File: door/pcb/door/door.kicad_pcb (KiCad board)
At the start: 2 copper layers, 73.2 x 35.1 mm, 43 parts, among them J1 USB_B_Micro, J2 Conn_01x06_Male, J3 DB9_Female_MountingHoles, J4 Conn_01x03_Male, J5 Screw_Terminal_01x02, J6 Screw_Terminal_01x02, U1 10uF, U2 STM32F303CBTx, U3 SN65HVD230, Y1 8 Mhz

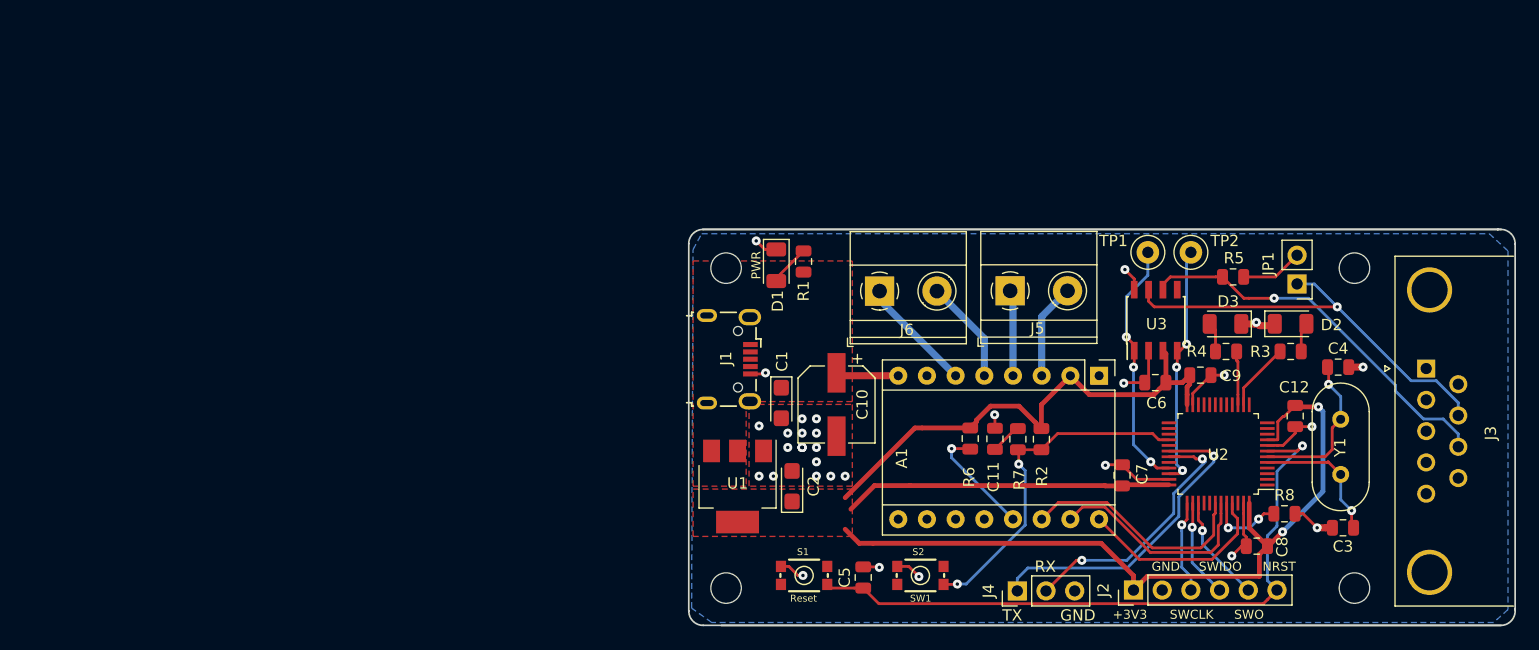
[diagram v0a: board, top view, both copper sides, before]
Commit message: recplaced usb micro jack with barrel-jack, reworked pcb layout
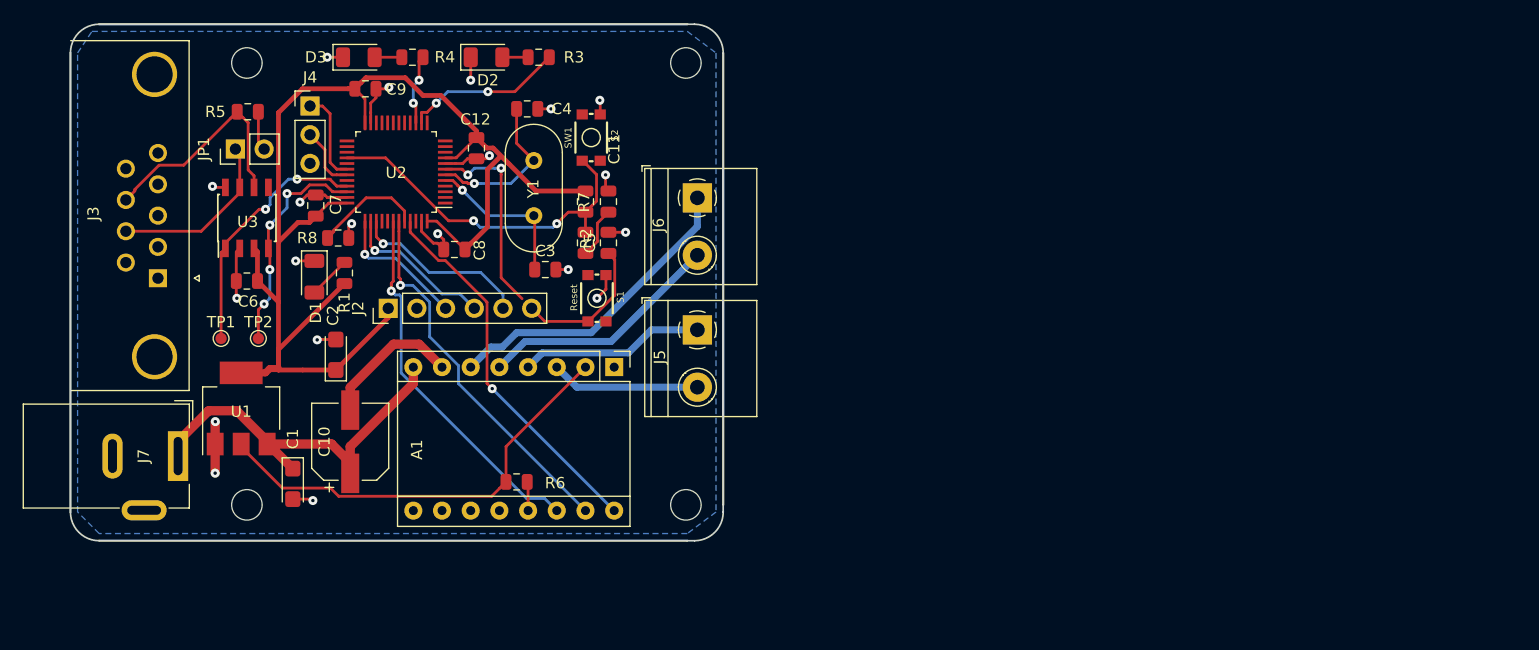
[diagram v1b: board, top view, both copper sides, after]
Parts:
- removed J1: USB_B_Micro, Connector_USB:USB_Micro-B_Wuerth_629105150521
- removed the REF** at (208.3, 121.7)
- removed the REF** at (208.3, 93.3)
- added J7: Power_in, Connector_BarrelJack:BarrelJack_Wuerth_6941xx301002, F.Cu at (104.1, 110.0)
- added REF**: MountingHole_2.7mm_M2.5, MountingHole:MountingHole_2.7mm_M2.5, F.Cu at (149.1, 114.3)
- added REF**: MountingHole_2.7mm_M2.5, MountingHole:MountingHole_2.7mm_M2.5, F.Cu at (149.1, 75.2)
- TP1, TP2: footprint TestPoint:TestPoint_Loop_D1.80mm_Drill1.0mm_Beaded -> TestPoint:TestPoint_Pad_D1.0mm
- moved J3 112.6 mm to (102.4, 94.2), turned to 270 degrees
- moved JP1 94.7 mm to (109.2, 82.8), turned to 90 degrees
- moved R5 88.4 mm to (110.3, 79.5)
- moved R8 87.3 mm to (118.3, 90.7)
- moved TP2 82.9 mm to (111.3, 99.6)
- moved TP1 82.4 mm to (108.0, 99.6)
- moved U3 81.0 mm to (110.2, 88.9)
- moved C6 80.9 mm to (110.2, 94.5)
- moved D3 80.3 mm to (120.1, 74.7), turned to 0 degrees
- moved C9 78.1 mm to (120.7, 77.5)
- moved U2 76.9 mm to (123.4, 84.8)
- moved R4 76.6 mm to (124.9, 74.7)
- moved C12 76.3 mm to (130.6, 82.7)
- moved J4 75.9 mm to (115.8, 79.0), turned to 0 degrees
- moved C8 75.7 mm to (128.6, 91.7)
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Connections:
- A1 pad 8: +5V -> +9V
- C1 pad 1: +5V -> +9V
- C10 pad 1: +5V -> +9V
- R1 pad 1: +5V -> +3V3
- U1 pad 3: +5V -> +9V
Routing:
- net +9V: track 0.00 -> 35.6 mm
- net NRST: track 58.8 -> 30.4 mm, vias 1 -> 2
- net /mcu/CANH: track 37.7 -> 15.5 mm, vias 1 -> 0
- net USART1_TX: track 28.4 -> 8.12 mm, vias 1 -> 0
- net USART1_RX: track 23.3 -> 5.67 mm, vias 2 -> 0
- net /motor/2B: track 10.3 -> 27.8 mm
- net DIR: track 17.6 -> 33.4 mm, vias 0 -> 1
- net STEP: track 19.3 -> 33.1 mm, vias 0 -> 1
- net /mcu/CANL: track 34.1 -> 20.5 mm, vias 1 -> 0
- net GND: track 47.1 -> 60.3 mm, vias 32 -> 20
- net /motor/2A: track 9.23 -> 21.6 mm
- net SLEEP: track 20.9 -> 32.9 mm, vias 0 -> 1
- net +3V3: track 143.1 -> 155.1 mm, vias 2 -> 0
- net /motor/1A: track 7.62 -> 16.4 mm
- net LED1: track 6.06 -> 14.2 mm, vias 0 -> 2
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- removed copper zone on F.Cu, net +3V3
- removed copper zone on F.Cu, net +5V
- removed copper zone on F.Cu, net GND
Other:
- board size 73.2 x 35.1 mm -> 57.8 x 45.7 mm
- net class +9V added: clearance 0.1524, trace_width 0.625, via_dia 0.8, via_drill 0.3
- board text removed: "+3V3"
- board text removed: "1A"
- board text removed: "1B"
- board text removed: "2A"
- board text removed: "2B"
- board text removed: "GND"
- board text removed: "NRST"
- board text removed: "PWR"
- board text removed: "RX"
- board text removed: "SWCLK"
- board text removed: "SWIDO"
- board text removed: "SWO"
- board text removed: "TX"
- board text removed: "Türsteuerung V0.1"

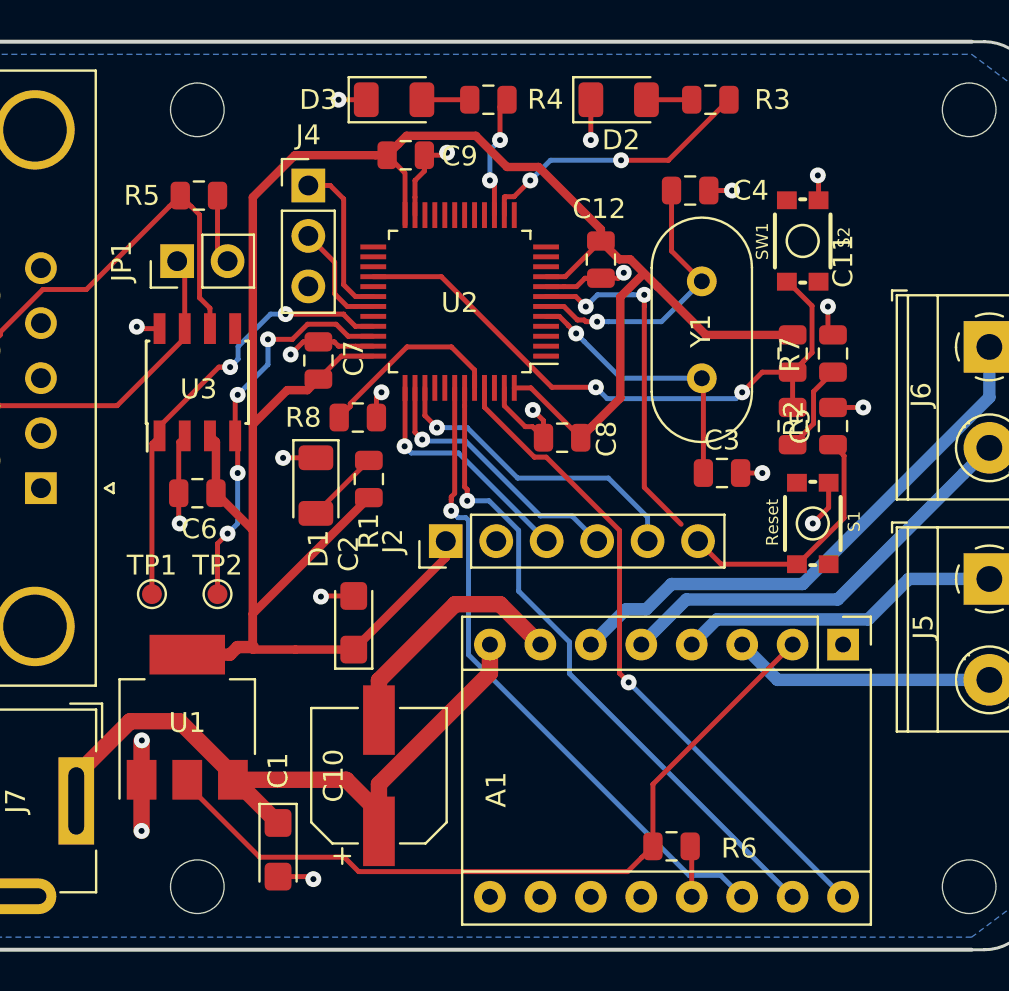
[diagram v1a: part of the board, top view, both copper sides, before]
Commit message: labeling and trackwidth
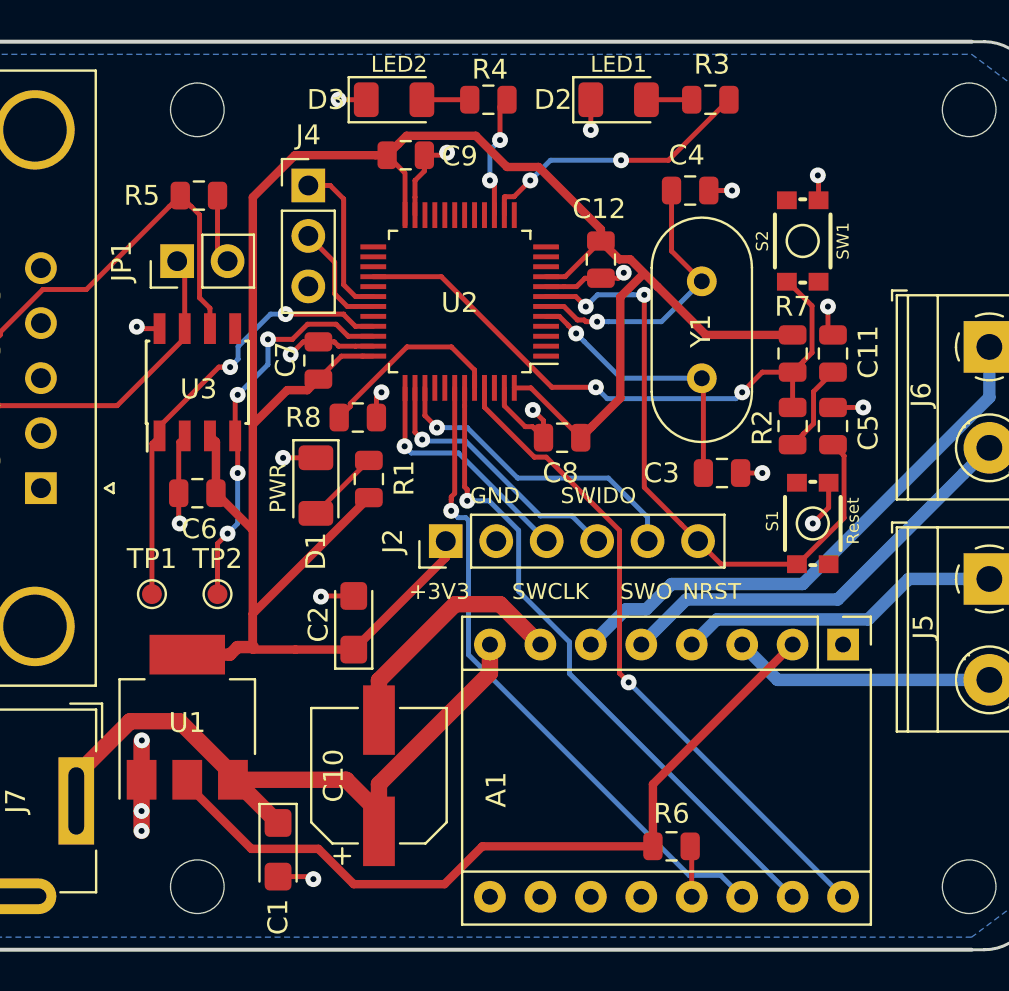
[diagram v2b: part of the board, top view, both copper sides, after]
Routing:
- net NRST: track 30.4 -> 31.6 mm
- net +3V3: track 155.1 -> 155.7 mm
- net GND: track 60.3 -> 59.8 mm, vias 20 -> 21
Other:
- board text added: "+3V3"
- board text added: "1A"
- board text added: "1B"
- board text added: "2A"
- board text added: "2B"
- board text added: "GND"
- board text added: "LED1"
- board text added: "LED2"
- board text added: "NRST"
- board text added: "PWR"
- board text added: "SWCLK"
- board text added: "SWIDO"
- board text added: "SWO"
- board text added: "door V0.2"

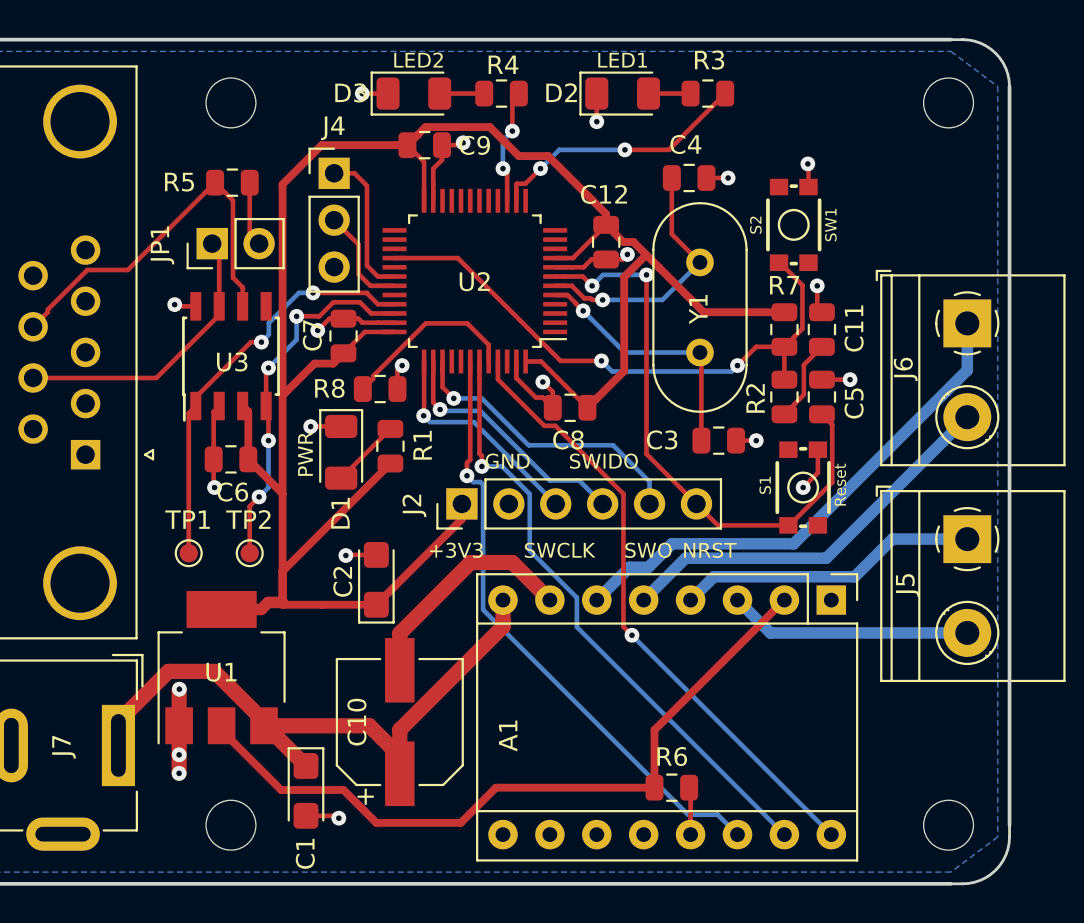
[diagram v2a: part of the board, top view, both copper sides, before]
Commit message: updated pcb ground plane layout
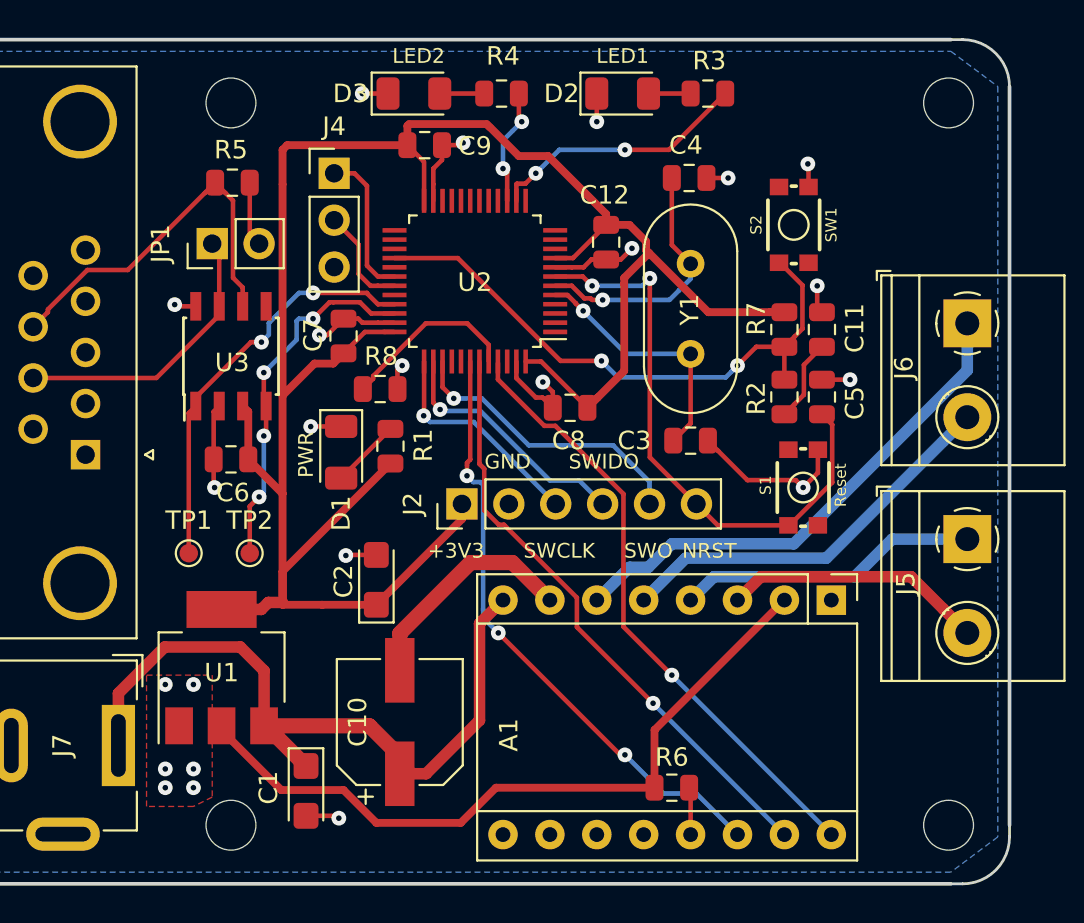
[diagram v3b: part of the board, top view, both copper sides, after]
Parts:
- moved C3 1.52 mm to (135.1, 93.5)
- moved Y1 0.51 mm to (135.1, 88.8)
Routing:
- net +9V: track 35.6 -> 41.5 mm
- net +3V3: track 155.7 -> 158.1 mm
- net /motor/1B: track 13.2 -> 14.2 mm
- net GND: track 59.8 -> 60.8 mm, vias 21 -> 23
- net Net-(C4-Pad1): track 14.8 -> 14.0 mm
- net LED2: track 6.26 -> 6.89 mm
- net SLEEP: track 32.9 -> 33.2 mm, vias 1 -> 3
- added copper zone on F.Cu, net GND

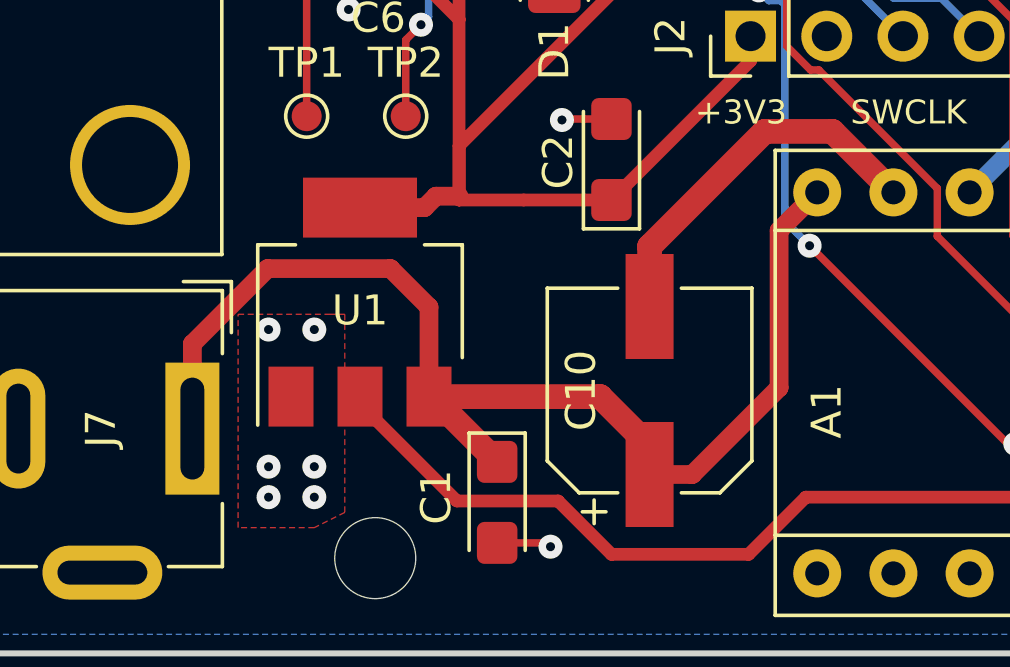
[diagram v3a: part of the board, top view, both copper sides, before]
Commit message: reverse voltage protection added
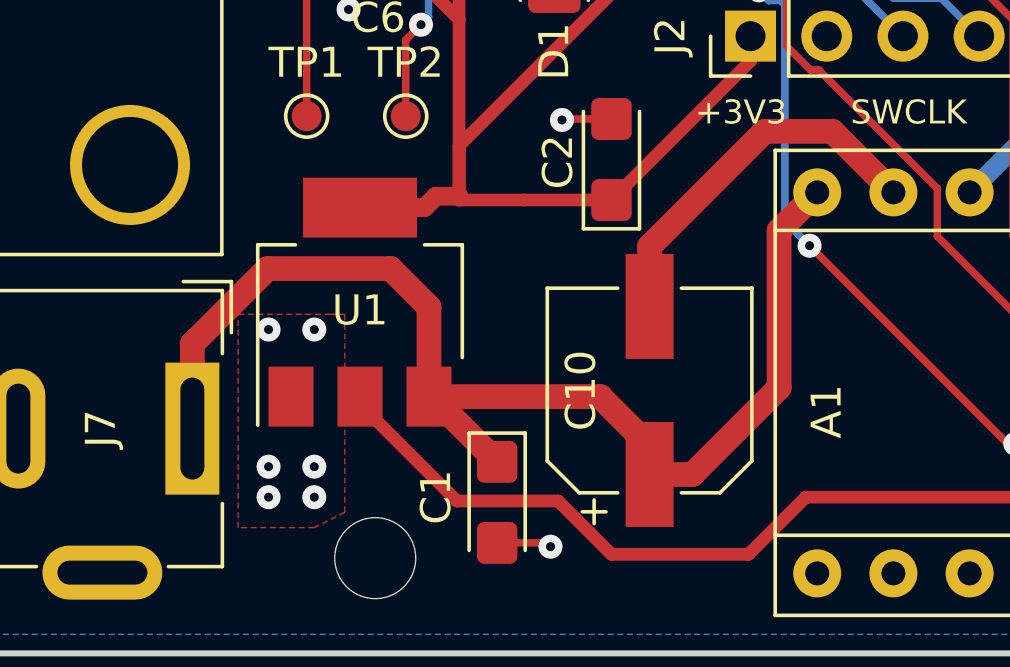
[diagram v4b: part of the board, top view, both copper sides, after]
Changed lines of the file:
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@@
       (rotate (xyz 0 0 0))
+    )
+    (model "/home/erik/Downloads/d-sub-9-polig-print.snapshot.7/D Sub 9 polig Print.STEP"
+      (offset (xyz -5.5 -9.5 6.5))
+      (scale (xyz 1 1 1))
+      (rotate (xyz -90 0 0))
     )
   )
@@
       (rotate (xyz 0 0 0))
     )
+    (model /home/erik/Downloads/terminal-block-connector-1.snapshot.7/WURTH_691216510002.STEP
+      (offset (xyz 2.5 0 0))
+      (scale (xyz 1 1 1))
+      (rotate (xyz -90 0 180))
+    )
   )
   (module TerminalBlock_Phoenix:TerminalBlock_Phoenix_MKDS-1,5-2-5.08_1x02_P5.08mm_Horizontal (layer F.Cu)
@@
       (rotate (xyz 0 0 0))
     )
+    (model /home/erik/Downloads/terminal-block-connector-1.snapshot.7/WURTH_691216510002.STEP
+      (offset (xyz 2.5 0 0))
+      (scale (xyz 1 1 1))
+      (rotate (xyz -90 0 180))
+    )
   )
   (module MountingHole:MountingHole_2.7mm_M2.5 (layer F.Cu)
@@
       (net 70 +9V))
     (model ${KISYS3DMOD}/Connector_BarrelJack.3dshapes/BarrelJack_Wuerth_6941xx301002.wrl
-      (at (xyz 0 0 0))
-      (scale (xyz 1 1 1))
-      (rotate (xyz 0 0 0))
+      (offset (xyz 8 1 0))
+      (scale (xyz 1 1 1))
+      (rotate (xyz 0 0 0))
+    )
+    (model /home/erik/Downloads/ej503b-connector-1.snapshot.2/EJ503B-ND.stp
+      (offset (xyz -4.5 -14 0))
+      (scale (xyz 1 1 1))
+      (rotate (xyz 0 0 90))
     )
   )
@@
   (segment (start 104.14 109.982) (end 104.14 108.682) (width 0.825) (layer F.Cu) (net 70))
   (segment (start 112.028 108.666) (end 112.028 108.916) (width 0.825) (layer F.Cu) (net 70))
-  (segment (start 112.028 105.932) (end 112.028 108.916) (width 0.625) (layer F.Cu) (net 70))
-  (segment (start 110.744 104.648) (end 112.028 105.932) (width 0.625) (layer F.Cu) (net 70))
-  (segment (start 106.649 104.648) (end 110.744 104.648) (width 0.625) (layer F.Cu) (net 70))
-  (segment (start 104.14 109.982) (end 104.14 107.157) (width 0.625) (layer F.Cu) (net 70))
-  (segment (start 104.14 107.157) (end 106.649 104.648) (width 0.625) (layer F.Cu) (net 70))
-  (segment (start 120.805 111.512) (end 123.698 108.619) (width 0.625) (layer F.Cu) (net 70))
-  (segment (start 119.38 111.512) (end 120.805 111.512) (width 0.625) (layer F.Cu) (net 70))
-  (segment (start 123.698 103.378) (end 124.968 102.108) (width 0.625) (layer F.Cu) (net 70))
-  (segment (start 123.698 108.619) (end 123.698 103.378) (width 0.625) (layer F.Cu) (net 70))
+  (segment (start 112.028 105.932) (end 112.028 108.916) (width 0.825) (layer F.Cu) (net 70))
+  (segment (start 110.744 104.648) (end 112.028 105.932) (width 0.825) (layer F.Cu) (net 70))
+  (segment (start 106.649 104.648) (end 110.744 104.648) (width 0.825) (layer F.Cu) (net 70))
+  (segment (start 104.14 109.982) (end 104.14 107.157) (width 0.825) (layer F.Cu) (net 70))
+  (segment (start 104.14 107.157) (end 106.649 104.648) (width 0.825) (layer F.Cu) (net 70))
+  (segment (start 120.805 111.512) (end 123.698 108.619) (width 0.825) (layer F.Cu) (net 70))
+  (segment (start 119.38 111.512) (end 120.805 111.512) (width 0.825) (layer F.Cu) (net 70))
+  (segment (start 123.698 103.378) (end 124.968 102.108) (width 0.825) (layer F.Cu) (net 70))
+  (segment (start 123.698 108.619) (end 123.698 103.378) (width 0.825) (layer F.Cu) (net 70))
   (zone (net 1) (net_name GND) (layer B.Cu) (hatch edge 0.508)
     (connect_pads (clearance 0.1524))
